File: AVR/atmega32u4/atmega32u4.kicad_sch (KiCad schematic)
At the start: 13 parts

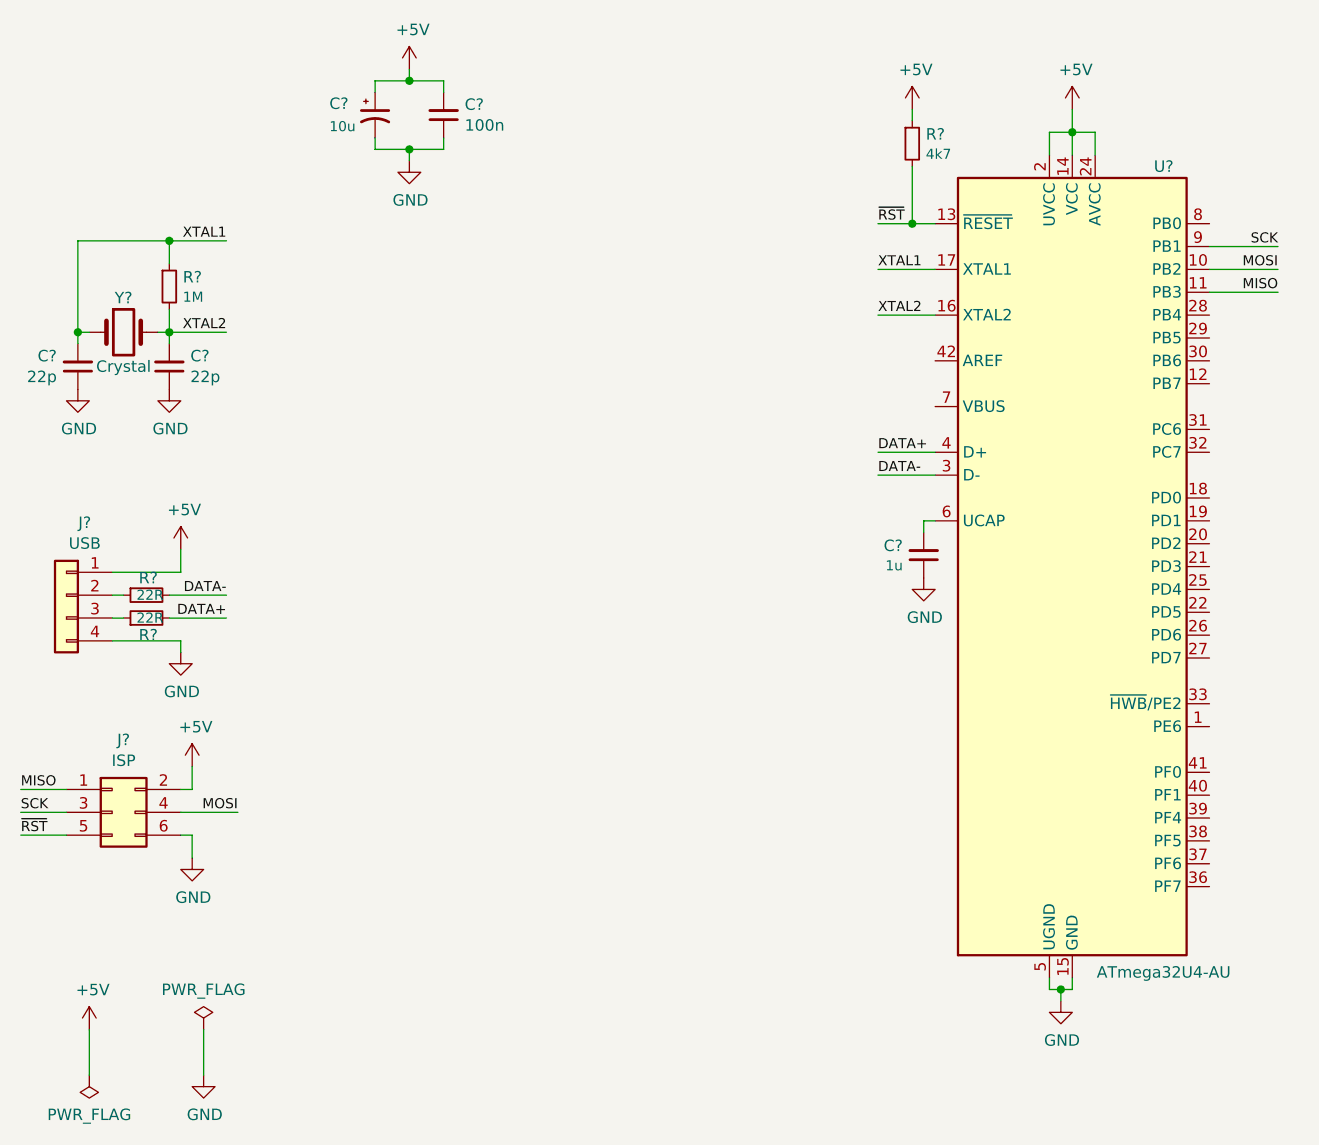
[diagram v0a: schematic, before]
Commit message: Fix grid alignment and update to KiCad 9
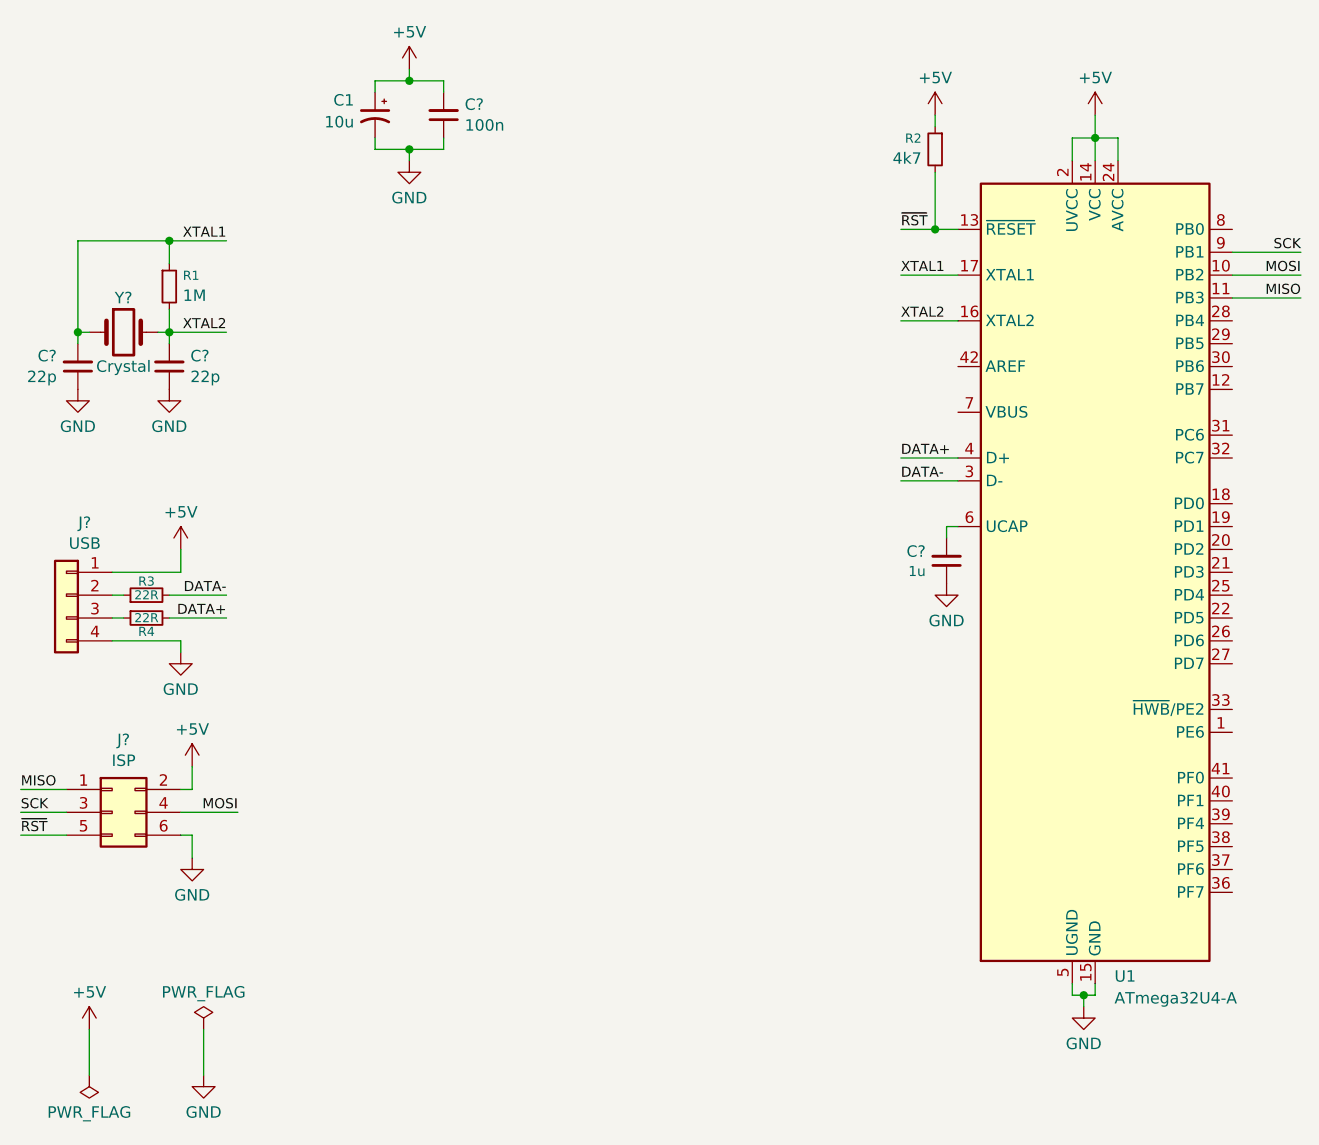
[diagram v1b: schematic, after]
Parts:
- removed C?: 10u, symbol Device:CP1_Small
- removed R?: 1M, symbol Device:R_Small
- removed R?: 4k7, symbol Device:R_Small
- removed R? (x2): 22R, symbol Device:R_Small
- removed U?: ATmega32U4-AU, Package_QFP:TQFP-44_10x10mm_P0.8mm, symbol atmega32u4-rescue:ATmega32U4-AU-MCU_Microchip_ATmega
- added C1: 10u, symbol Device:C_Polarized_Small_US
- added R1: 1M, symbol Device:R_Small
- added R2: 4k7, symbol Device:R_Small
- added R3, R4: 22R, symbol Device:R_Small
- added U1: ATmega32U4-A, Package_QFP:TQFP-44_10x10mm_P0.8mm, symbol MCU_Microchip_ATmega:ATmega32U4-A
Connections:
- net +5V: now also C1.1, R2.1, U1.14 (VCC), U1.2 (UVCC), U1.24 (AVCC), U1.34 (VCC), U1.44 (AVCC)
- net DATA+: now also R4.2, U1.4 (D+)
- net DATA-: now also R3.2, U1.3 (D-)
- net GND: now also C1.2, U1.15 (GND), U1.23 (GND), U1.35 (GND), U1.43 (GND), U1.5 (UGND)
- net MISO: now also U1.11 (PB3)
- net MOSI: now also U1.10 (PB2)
- net SCK: now also U1.9 (PB1)
- net XTAL1: now also R1.1, U1.17 (XTAL1)
- net XTAL2: now also R1.2, U1.16 (XTAL2)
- net ~{RST}: now also R2.2, U1.13 (~{RESET})
- net at C?.2: now also U1.6 (UCAP)
- net at J?.2 (Pin_2): now also R3.1
- net at J?.3 (Pin_3): now also R4.1
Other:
- moved on the sheet: C?
